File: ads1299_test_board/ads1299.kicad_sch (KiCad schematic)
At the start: 20 parts, among them U1 ADS1299

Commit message: charger circuit
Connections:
- net agnd renamed GND
- net dgnd renamed GNDD

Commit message: usb, esp32 s3 wroom 1
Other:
- moved on the sheet: C1, C10, C11, C6, C7, C8, C9

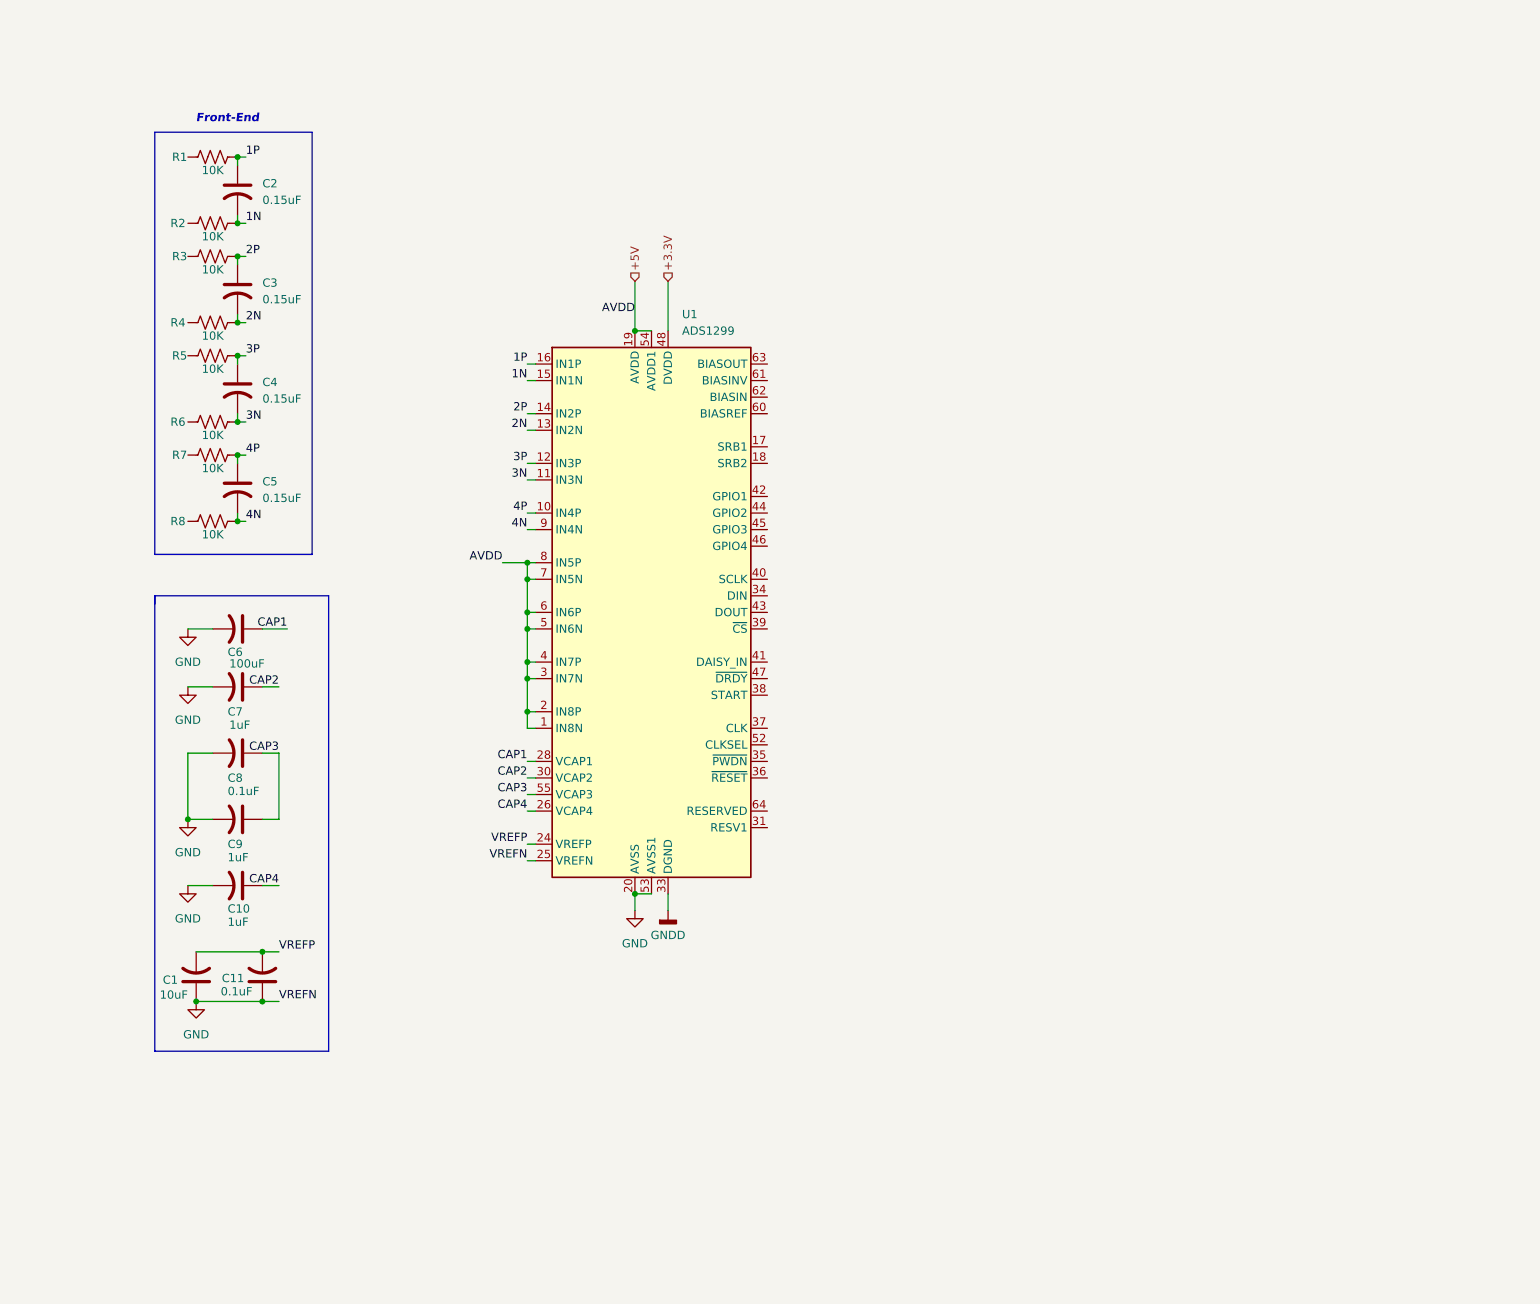
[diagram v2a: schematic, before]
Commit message: usb charge and power circuit switch
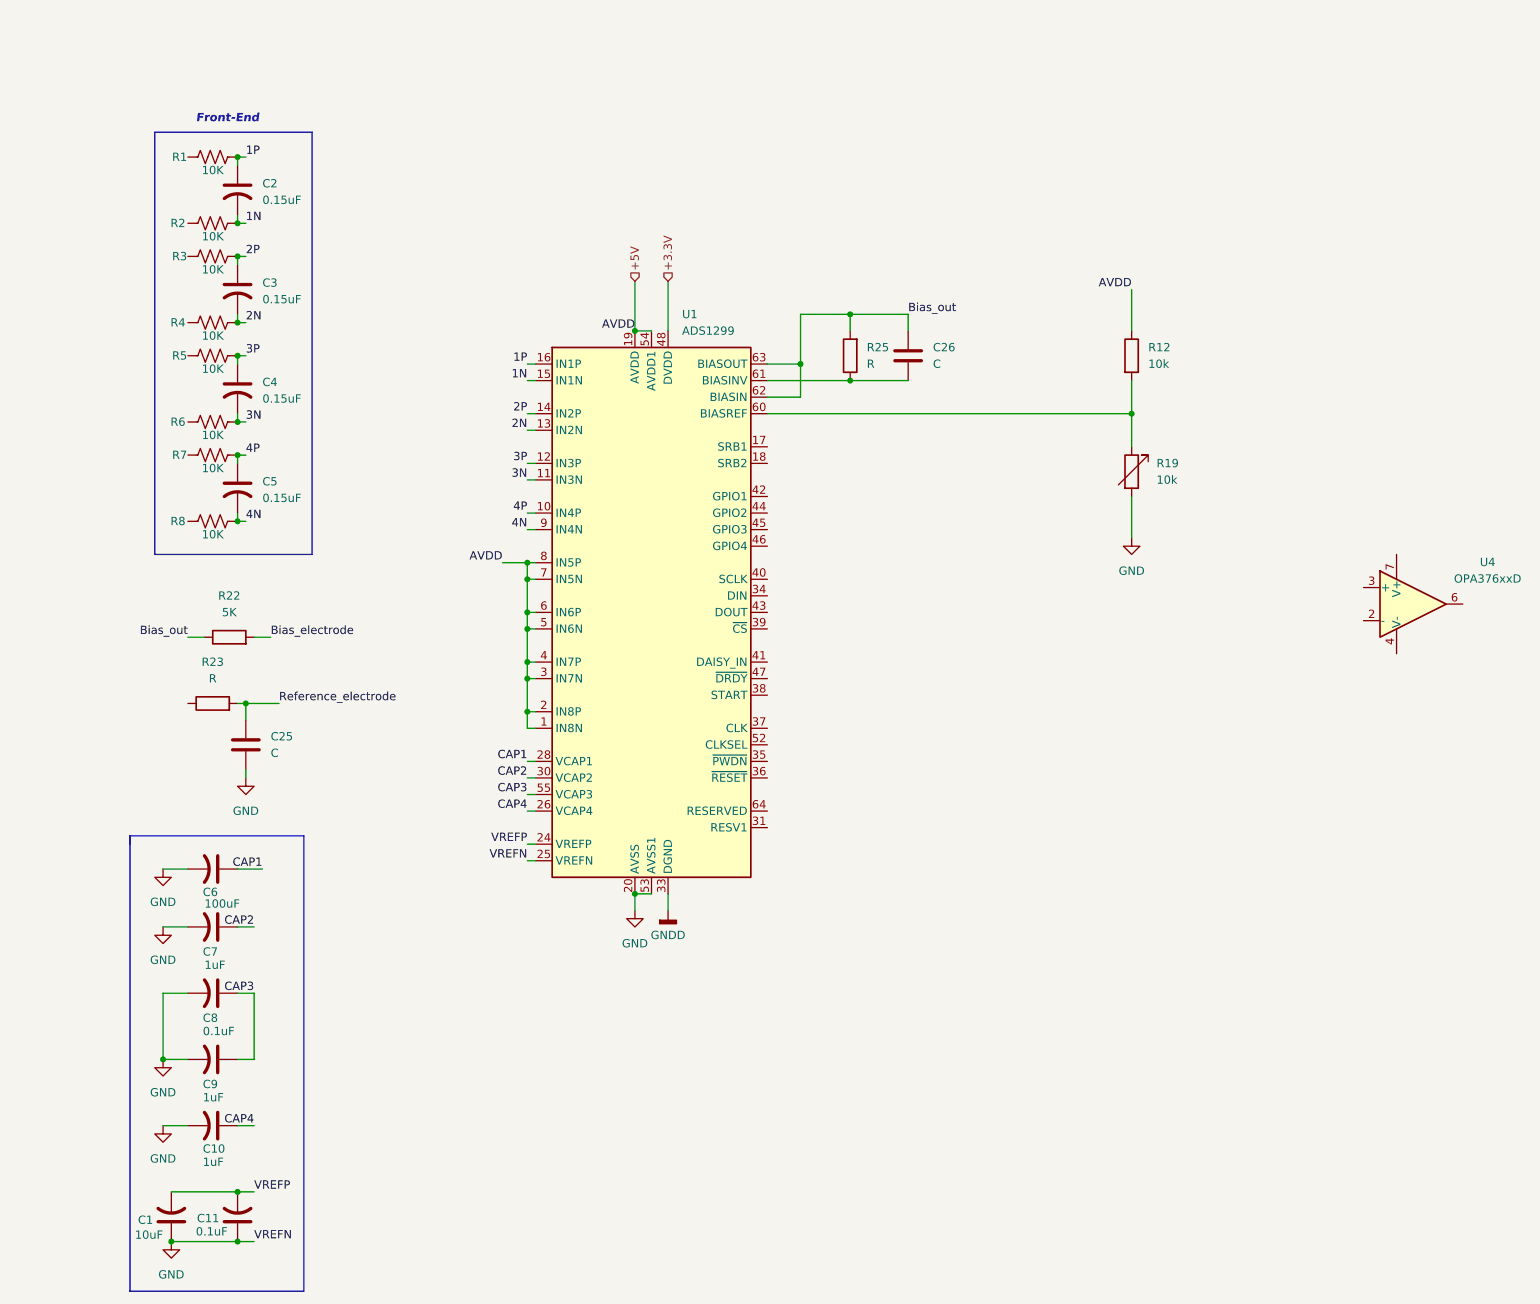
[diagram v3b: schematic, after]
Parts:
- added C25, C26: C, symbol Device:C
- added R12: 10k, symbol Device:R
- added R19: 10k, symbol Device:R_Variable
- added R22: 5K, symbol Device:R
- added R23, R25: R, symbol Device:R
- added U4: OPA376xxD, Package_SO:SOIC-8_3.9x4.9mm_P1.27mm, symbol Amplifier_Operational:OPA376xxD
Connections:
- net +5V: now also R12.1
- net GND: now also C25.2, R19.2
- net at U1.60 (BIASREF): now also R12.2, R19.1
- net at U1.61 (BIASINV): now also C26.2, R25.1
- net Bias_out: now reaches U1.62 (BIASIN)
- net Bias_out: now also U1.63 (BIASOUT), C26.1, R22.1, R25.2
- new net Bias_electrode: R22.2
- new net Reference_electrode: C25.1, R23.2
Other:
- moved on the sheet: C1, C10, C11, C6, C7, C8, C9

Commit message: work on ads1299 schematic
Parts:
- added R26: 10k, symbol Device:R
- added TP1: TestPoint, symbol Connector:TestPoint
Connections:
- net +3.3V: now also R26.2
- net Bias_out: now also C26.2, R25.1; no longer C26.1, R25.2
- net GNDD: now also U1.41 (DAISY_IN)
- net DIN: now reaches U1.34 (DIN)
- net Power_ads1299: now reaches U1.35 (~{PWDN})
- net Reset_ads1299: now reaches U1.36 (~{RESET})
- net at U1.37 (CLK): now also TP1.1
- net Start: now reaches U1.38 (START)
- net CS: now reaches U1.39 (~{CS})
- net SCLK: now reaches U1.40 (SCLK)
- net DOUT: now reaches U1.43 (DOUT)
- net DRDY: now reaches U1.47 (~{DRDY})
- net at U1.52 (CLKSEL): now also R26.1
- new net: C26.1, R25.2, U1.61 (BIASINV)
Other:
- moved on the sheet: C26, R12, R19, R25

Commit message: GPIO, SRB
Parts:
- removed C25: C, symbol Device:C
- removed R23: R, symbol Device:R
- added C28: 1uF, symbol Device:C
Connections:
- net +5V: now also U4.7 (V+), C28.1
- net GND: now also U1.18 (SRB2), U4.4 (V-), C28.2
- net SRB1: now reaches U1.17 (SRB1)
- net SRB1: now also U4.2 (-), U4.6
- net GPIO1: now reaches U1.42 (GPIO1)
- net GPIO2: now reaches U1.44 (GPIO2)
- net GPIO3: now reaches U1.45 (GPIO3)
- net GPIO4: now reaches U1.46 (GPIO4)
- net Ref_electrode: now reaches U4.3 (+)
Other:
- moved on the sheet: C2, C26, C3, C4, C5, R1, R12, R19, R2, R22, R25, R26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

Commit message: updates
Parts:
- C1, C10, C11, C28, C7, C8, C9, R22: footprint (none) -> Capacitor_SMD:C_0402_1005Metric_Pad0.74x0.62mm_HandSolder
- C2, C3, C4, C5: footprint (none) -> Capacitor_SMD:C_0603_1608Metric_Pad1.08x0.95mm_HandSolder
- C6: footprint (none) -> Capacitor_SMD:C_1206_3216Metric_Pad1.33x1.80mm_HandSolder
- R1, R12, R19, R2, R26, R3, R4, R5, R6, R7, R8: footprint (none) -> Resistor_SMD:R_0402_1005Metric_Pad0.72x0.64mm_HandSolder
- TP1: footprint (none) -> TestPoint:TestPoint_Pad_D1.5mm
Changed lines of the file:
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@@
 			)
 		)
-		(property "Footprint" ""
+		(property "Footprint" "Capacitor_SMD:C_0402_1005Metric_Pad0.74x0.62mm_HandSolder"
 			(at 29.21 149.86 0)
 			(hide yes)
@@
 			)
 		)
-		(property "Footprint" ""
+		(property "Footprint" "Capacitor_SMD:C_0402_1005Metric_Pad0.74x0.62mm_HandSolder"
 			(at 29.21 160.02 0)
 			(hide yes)
@@
 			)
 		)
-		(property "Footprint" ""
+		(property "Footprint" "Capacitor_SMD:C_0402_1005Metric_Pad0.74x0.62mm_HandSolder"
 			(at 29.21 170.18 0)
 			(hide yes)
@@
 			)
 		)
-		(property "Footprint" ""
+		(property "Footprint" "Capacitor_SMD:C_0402_1005Metric_Pad0.74x0.62mm_HandSolder"
 			(at 33.02 184.15 0)
 			(hide yes)
@@
 			)
 		)
-		(property "Footprint" ""
+		(property "Footprint" "Resistor_SMD:R_0402_1005Metric_Pad0.72x0.64mm_HandSolder"
 			(at 186.182 45.72 90)
 			(hide yes)
@@
 			)
 		)
-		(property "Footprint" ""
+		(property "Footprint" "Resistor_SMD:R_0402_1005Metric_Pad0.72x0.64mm_HandSolder"
 			(at 156.21 107.188 90)
 			(hide yes)
@@
 			)
 		)
-		(property "Footprint" ""
+		(property "Footprint" "Capacitor_SMD:C_0402_1005Metric_Pad0.74x0.62mm_HandSolder"
 			(at 22.86 184.15 0)
 			(hide yes)
@@
 			)
 		)
-		(property "Footprint" ""
+		(property "Footprint" "Resistor_SMD:R_0402_1005Metric_Pad0.72x0.64mm_HandSolder"
 			(at 25.654 85.344 90)
 			(hide yes)
@@
 			)
 		)
-		(property "Footprint" ""
+		(property "Footprint" "Resistor_SMD:R_0402_1005Metric_Pad0.72x0.64mm_HandSolder"
 			(at 25.654 75.184 90)
 			(hide yes)
@@
 			)
 		)
-		(property "Footprint" ""
+		(property "Footprint" "Capacitor_SMD:C_0603_1608Metric_Pad1.08x0.95mm_HandSolder"
 			(at 29.21 81.28 0)
 			(hide yes)
@@
 			)
 		)
-		(property "Footprint" ""
+		(property "Footprint" "Resistor_SMD:R_0402_1005Metric_Pad0.72x0.64mm_HandSolder"
 			(at 25.654 115.824 90)
 			(hide yes)
@@
 			)
 		)
-		(property "Footprint" ""
+		(property "Footprint" "Resistor_SMD:R_0402_1005Metric_Pad0.72x0.64mm_HandSolder"
 			(at 25.654 70.104 90)
 			(hide yes)
@@
 			)
 		)
-		(property "Footprint" ""
+		(property "Footprint" "Resistor_SMD:R_0402_1005Metric_Pad0.72x0.64mm_HandSolder"
 			(at 25.654 90.424 90)
 			(hide yes)
@@
 			)
 		)
-		(property "Footprint" ""
+		(property "Footprint" "Capacitor_SMD:C_0402_1005Metric_Pad0.74x0.62mm_HandSolder"
 			(at 36.83 37.592 90)
 			(hide yes)
@@
 			)
 		)
-		(property "Footprint" ""
+		(property "Footprint" "Resistor_SMD:R_0402_1005Metric_Pad0.72x0.64mm_HandSolder"
 			(at 186.182 63.5 90)
 			(hide yes)
@@
 			)
 		)
-		(property "Footprint" ""
+		(property "Footprint" "Capacitor_SMD:C_0603_1608Metric_Pad1.08x0.95mm_HandSolder"
 			(at 29.21 96.52 0)
 			(hide yes)
@@
 			)
 		)
-		(property "Footprint" ""
+		(property "Footprint" "Resistor_SMD:R_0402_1005Metric_Pad0.72x0.64mm_HandSolder"
 			(at 25.654 105.664 90)
 			(hide yes)
@@
 			)
 		)
-		(property "Footprint" ""
+		(property "Footprint" "Capacitor_SMD:C_1206_3216Metric_Pad1.33x1.80mm_HandSolder"
 			(at 29.21 130.81 0)
 			(hide yes)
@@
 			)
 		)
-		(property "Footprint" ""
+		(property "Footprint" "TestPoint:TestPoint_Pad_D1.5mm"
 			(at 167.64 101.6 0)
 			(hide yes)
@@
 			)
 		)
-		(property "Footprint" ""
+		(property "Footprint" "Resistor_SMD:R_0402_1005Metric_Pad0.72x0.64mm_HandSolder"
 			(at 25.654 59.944 90)
 			(hide yes)
@@
 			)
 		)
-		(property "Footprint" ""
+		(property "Footprint" "Capacitor_SMD:C_0402_1005Metric_Pad0.74x0.62mm_HandSolder"
 			(at 69.5452 167.64 0)
 			(hide yes)
@@
 			)
 		)
-		(property "Footprint" ""
+		(property "Footprint" "Capacitor_SMD:C_0402_1005Metric_Pad0.74x0.62mm_HandSolder"
 			(at 29.21 139.7 0)
 			(hide yes)
@@
 			)
 		)
-		(property "Footprint" ""
+		(property "Footprint" "Capacitor_SMD:C_0603_1608Metric_Pad1.08x0.95mm_HandSolder"
 			(at 29.21 111.76 0)
 			(hide yes)
@@
 			)
 		)
-		(property "Footprint" ""
+		(property "Footprint" "Capacitor_SMD:C_0603_1608Metric_Pad1.08x0.95mm_HandSolder"
 			(at 29.21 66.04 0)
 			(hide yes)
@@
 			)
 		)
-		(property "Footprint" ""
+		(property "Footprint" "Resistor_SMD:R_0402_1005Metric_Pad0.72x0.64mm_HandSolder"
 			(at 25.654 100.584 90)
 			(hide yes)
